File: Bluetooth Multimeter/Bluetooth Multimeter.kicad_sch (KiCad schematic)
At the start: 33 parts, among them J1 V/Ohm, J2 Com, J3 mA, J4 A, J5 Parallel Prot, J6 3.3V, J7 GND, K1 Low Range, K2 Medium Range, K3 High Range, K4 UH Range (Ohm Only), K5 V/Ohm Switch, U1 ItsyBitsy_NRF52840_Big

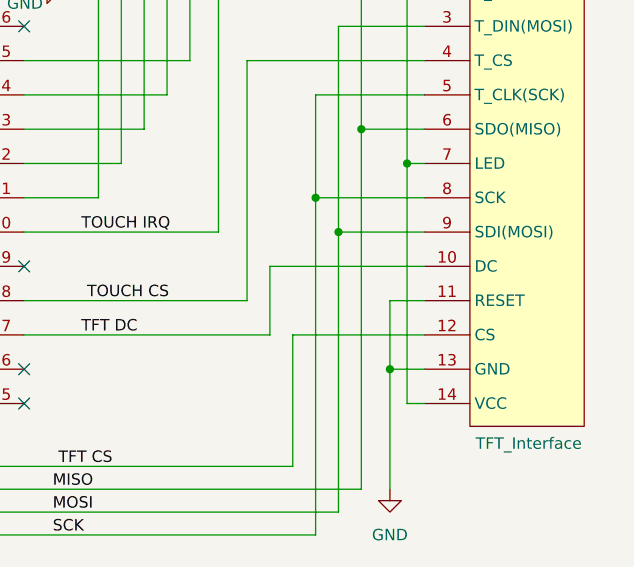
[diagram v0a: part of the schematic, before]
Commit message: fixed itsybitsy footprint and lcd connection
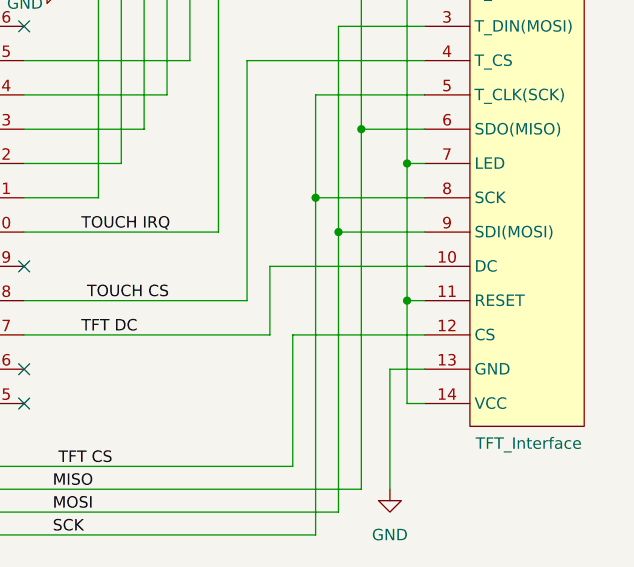
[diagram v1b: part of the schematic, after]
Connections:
- net +3.3V: now also DS1.11 (RESET)
- net GND: no longer DS1.11 (RESET)
- net Speaker Control: no longer U1.
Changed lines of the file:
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@@
   (junction (at 104.775 177.165) (diameter 0) (color 0 0 0 0)
   )
-  (junction (at 231.775 111.76) (diameter 0) (color 0 0 0 0)
-  )
   (junction (at 93.98 28.575) (diameter 0) (color 0 0 0 0)
   )
@@
   )
   (junction (at 107.95 167.005) (diameter 0) (color 0 0 0 0)
+  )
+  (junction (at 233.68 104.14) (diameter 0) (color 0 0 0 0)
   )
   (junction (at 120.65 167.005) (diameter 0) (color 0 0 0 0)
@@
     (stroke (width 0) (type default))
   )
-  (wire (pts (xy 231.775 104.14) (xy 231.775 111.76))
-    (stroke (width 0) (type default))
-  )
   (wire (pts (xy 153.67 100.33) (xy 163.195 100.33))
     (stroke (width 0) (type default))
@@
     (stroke (width 0) (type default))
   )
-  (wire (pts (xy 235.585 104.14) (xy 231.775 104.14))
+  (wire (pts (xy 235.585 104.14) (xy 233.68 104.14))
     (stroke (width 0) (type default))
   )
@@
     (stroke (width 0) (type default))
   )
-  (wire (pts (xy 233.68 88.9) (xy 233.68 115.57))
+  (wire (pts (xy 233.68 88.9) (xy 233.68 104.14))
     (stroke (width 0) (type default))
   )
@@
   )
   (wire (pts (xy 158.115 127.635) (xy 226.06 127.635))
+    (stroke (width 0) (type default))
+  )
+  (wire (pts (xy 233.68 104.14) (xy 233.68 115.57))
     (stroke (width 0) (type default))
   )
@@
       (effects (font (size 1.27 1.27)) hide)
     )
-    (pin "")
     (pin "1")
     (pin "10")

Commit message: pcb modifications based on first shop board
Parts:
- D1, D2, D3, D4: footprint Diode_THT:D_DO-41_SOD81_P10.16mm_Horizontal -> Diode_THT:D_DO-41_SOD81_P7.62mm_Horizontal
- D5, D6, D7, D8, D9: footprint Diode_THT:D_DO-35_SOD27_P7.62mm_Horizontal -> 502ProjectFootprints:D_DO-35_SOD27_P5.08mm_Horizontal
- DS1: footprint 502ProjectFootprints:PinHeader_1x14_P2.54mm_Vertical_H0.9mm -> 502ProjectFootprints:PinHeader_1x14_P2.54mm_Vertical_H1.0
- F2: footprint 502ProjectFootprints:LF124041_4 -> 502ProjectFootprints:LF124041_6
- J1, J2, J3, J4, J6, J7: footprint 502ProjectFootprints:PinHeader_1x01_P2.54mm_Vertical_H0.8mm -> 502ProjectFootprints:PinHeader_1x01_P2.54mm_Vertical_H0.9mm
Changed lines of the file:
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@@
       (effects (font (size 1.27 1.27)) (justify left))
     )
-    (property "Footprint" "Diode_THT:D_DO-35_SOD27_P7.62mm_Horizontal" (at 120.015 127 0)
+    (property "Footprint" "502ProjectFootprints:D_DO-35_SOD27_P5.08mm_Horizontal" (at 120.015 127 0)
       (effects (font (size 1.27 1.27)) hide)
     )
@@
       (effects (font (size 1.27 1.27)) (justify left))
     )
-    (property "Footprint" "Diode_THT:D_DO-35_SOD27_P7.62mm_Horizontal" (at 87.63 143.51 0)
+    (property "Footprint" "502ProjectFootprints:D_DO-35_SOD27_P5.08mm_Horizontal" (at 87.63 143.51 0)
       (effects (font (size 1.27 1.27)) hide)
     )
@@
       (effects (font (size 1.27 1.27)))
     )
-    (property "Footprint" "502ProjectFootprints:PinHeader_1x01_P2.54mm_Vertical_H0.8mm" (at 82.55 153.035 0)
+    (property "Footprint" "502ProjectFootprints:PinHeader_1x01_P2.54mm_Vertical_H0.9mm" (at 82.55 153.035 0)
       (effects (font (size 1.27 1.27)) hide)
     )
@@
       (effects (font (size 1.27 1.27)) (justify left))
     )
-    (property "Footprint" "Diode_THT:D_DO-35_SOD27_P7.62mm_Horizontal" (at 120.015 90.17 0)
+    (property "Footprint" "502ProjectFootprints:D_DO-35_SOD27_P5.08mm_Horizontal" (at 120.015 90.17 0)
       (effects (font (size 1.27 1.27)) hide)
     )
@@
       (effects (font (size 1.27 1.27)) (justify left))
     )
-    (property "Footprint" "502ProjectFootprints:PinHeader_1x14_P2.54mm_Vertical_H0.9mm" (at 239.395 59.69 0)
+    (property "Footprint" "502ProjectFootprints:PinHeader_1x14_P2.54mm_Vertical_H1.0" (at 239.395 59.69 0)
       (effects (font (size 1.27 1.27)) hide)
     )
@@
       (effects (font (size 1.27 1.27)) (justify left))
     )
-    (property "Footprint" "Diode_THT:D_DO-41_SOD81_P10.16mm_Horizontal" (at 114.3 161.29 0)
+    (property "Footprint" "Diode_THT:D_DO-41_SOD81_P7.62mm_Horizontal" (at 114.3 161.29 0)
       (effects (font (size 1.27 1.27)) hide)
     )
@@
       (effects (font (size 1.27 1.27)) (justify left))
     )
-    (property "Footprint" "Diode_THT:D_DO-41_SOD81_P10.16mm_Horizontal" (at 142.875 161.29 0)
+    (property "Footprint" "Diode_THT:D_DO-41_SOD81_P7.62mm_Horizontal" (at 142.875 161.29 0)
       (effects (font (size 1.27 1.27)) hide)
     )
@@
       (effects (font (size 1.27 1.27)) (justify left))
     )
-    (property "Footprint" "Diode_THT:D_DO-41_SOD81_P10.16mm_Horizontal" (at 120.65 161.29 0)
+    (property "Footprint" "Diode_THT:D_DO-41_SOD81_P7.62mm_Horizontal" (at 120.65 161.29 0)
       (effects (font (size 1.27 1.27)) hide)
     )
@@
       (effects (font (size 1.27 1.27)) (justify left))
     )
-    (property "Footprint" "Diode_THT:D_DO-41_SOD81_P10.16mm_Horizontal" (at 136.525 161.29 0)
+    (property "Footprint" "Diode_THT:D_DO-41_SOD81_P7.62mm_Horizontal" (at 136.525 161.29 0)
       (effects (font (size 1.27 1.27)) hide)
     )
@@
       (effects (font (size 1.27 1.27)))
     )
-    (property "Footprint" "502ProjectFootprints:PinHeader_1x01_P2.54mm_Vertical_H0.8mm" (at 82.55 167.005 0)
+    (property "Footprint" "502ProjectFootprints:PinHeader_1x01_P2.54mm_Vertical_H0.9mm" (at 82.55 167.005 0)
       (effects (font (size 1.27 1.27)) hide)
     )
@@
       (effects (font (size 1.27 1.27)))
     )
-    (property "Footprint" "502ProjectFootprints:PinHeader_1x01_P2.54mm_Vertical_H0.8mm" (at 29.21 24.13 0)
+    (property "Footprint" "502ProjectFootprints:PinHeader_1x01_P2.54mm_Vertical_H0.9mm" (at 29.21 24.13 0)
       (effects (font (size 1.27 1.27)) hide)
     )
@@
       (effects (font (size 1.27 1.27)))
     )
-    (property "Footprint" "502ProjectFootprints:PinHeader_1x01_P2.54mm_Vertical_H0.8mm" (at 29.21 30.48 0)
+    (property "Footprint" "502ProjectFootprints:PinHeader_1x01_P2.54mm_Vertical_H0.9mm" (at 29.21 30.48 0)
       (effects (font (size 1.27 1.27)) hide)
     )
@@
       (effects (font (size 1.27 1.27)))
     )
-    (property "Footprint" "502ProjectFootprints:PinHeader_1x01_P2.54mm_Vertical_H0.8mm" (at 82.55 177.165 0)
+    (property "Footprint" "502ProjectFootprints:PinHeader_1x01_P2.54mm_Vertical_H0.9mm" (at 82.55 177.165 0)
       (effects (font (size 1.27 1.27)) hide)
     )
@@
       (effects (font (size 1.27 1.27)) (justify left))
     )
-    (property "Footprint" "Diode_THT:D_DO-35_SOD27_P7.62mm_Horizontal" (at 120.015 54.61 0)
+    (property "Footprint" "502ProjectFootprints:D_DO-35_SOD27_P5.08mm_Horizontal" (at 120.015 54.61 0)
       (effects (font (size 1.27 1.27)) hide)
     )
@@
       (effects (font (size 1.27 1.27)))
     )
-    (property "Footprint" "502ProjectFootprints:LF124041_4" (at 92.075 172.085 0)
+    (property "Footprint" "502ProjectFootprints:LF124041_6" (at 92.075 172.085 0)
       (effects (font (size 1.27 1.27)) hide)
     )
@@
       (effects (font (size 1.27 1.27)) (justify left))
     )
-    (property "Footprint" "Diode_THT:D_DO-35_SOD27_P7.62mm_Horizontal" (at 120.015 22.86 0)
+    (property "Footprint" "502ProjectFootprints:D_DO-35_SOD27_P5.08mm_Horizontal" (at 120.015 22.86 0)
       (effects (font (size 1.27 1.27)) hide)
     )
@@
       (effects (font (size 1.27 1.27)))
     )
-    (property "Footprint" "502ProjectFootprints:PinHeader_1x01_P2.54mm_Vertical_H0.8mm" (at 83.185 28.575 0)
-      (effects (font (size 1.27 1.27)) hide)
-    )
+    (property "Footprint" "502ProjectFootprints:PinHeader_1x01_P2.54mm_Vertical_H0.9mm" (at 83.185 28.575 0)
+      (effects (font (size 1.27 1.27)) hide)
+    )

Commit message: finalized rev 2 board to be milled
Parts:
- F1: footprint 502ProjectFootprints:LF124061_1 -> 502ProjectFootprints:LF124061_3
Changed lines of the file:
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@@
       (effects (font (size 1.27 1.27)))
     )
-    (property "Footprint" "502ProjectFootprints:LF124061_1" (at 92.075 161.925 0)
+    (property "Footprint" "502ProjectFootprints:LF124061_3" (at 92.075 161.925 0)
       (effects (font (size 1.27 1.27)) hide)
     )

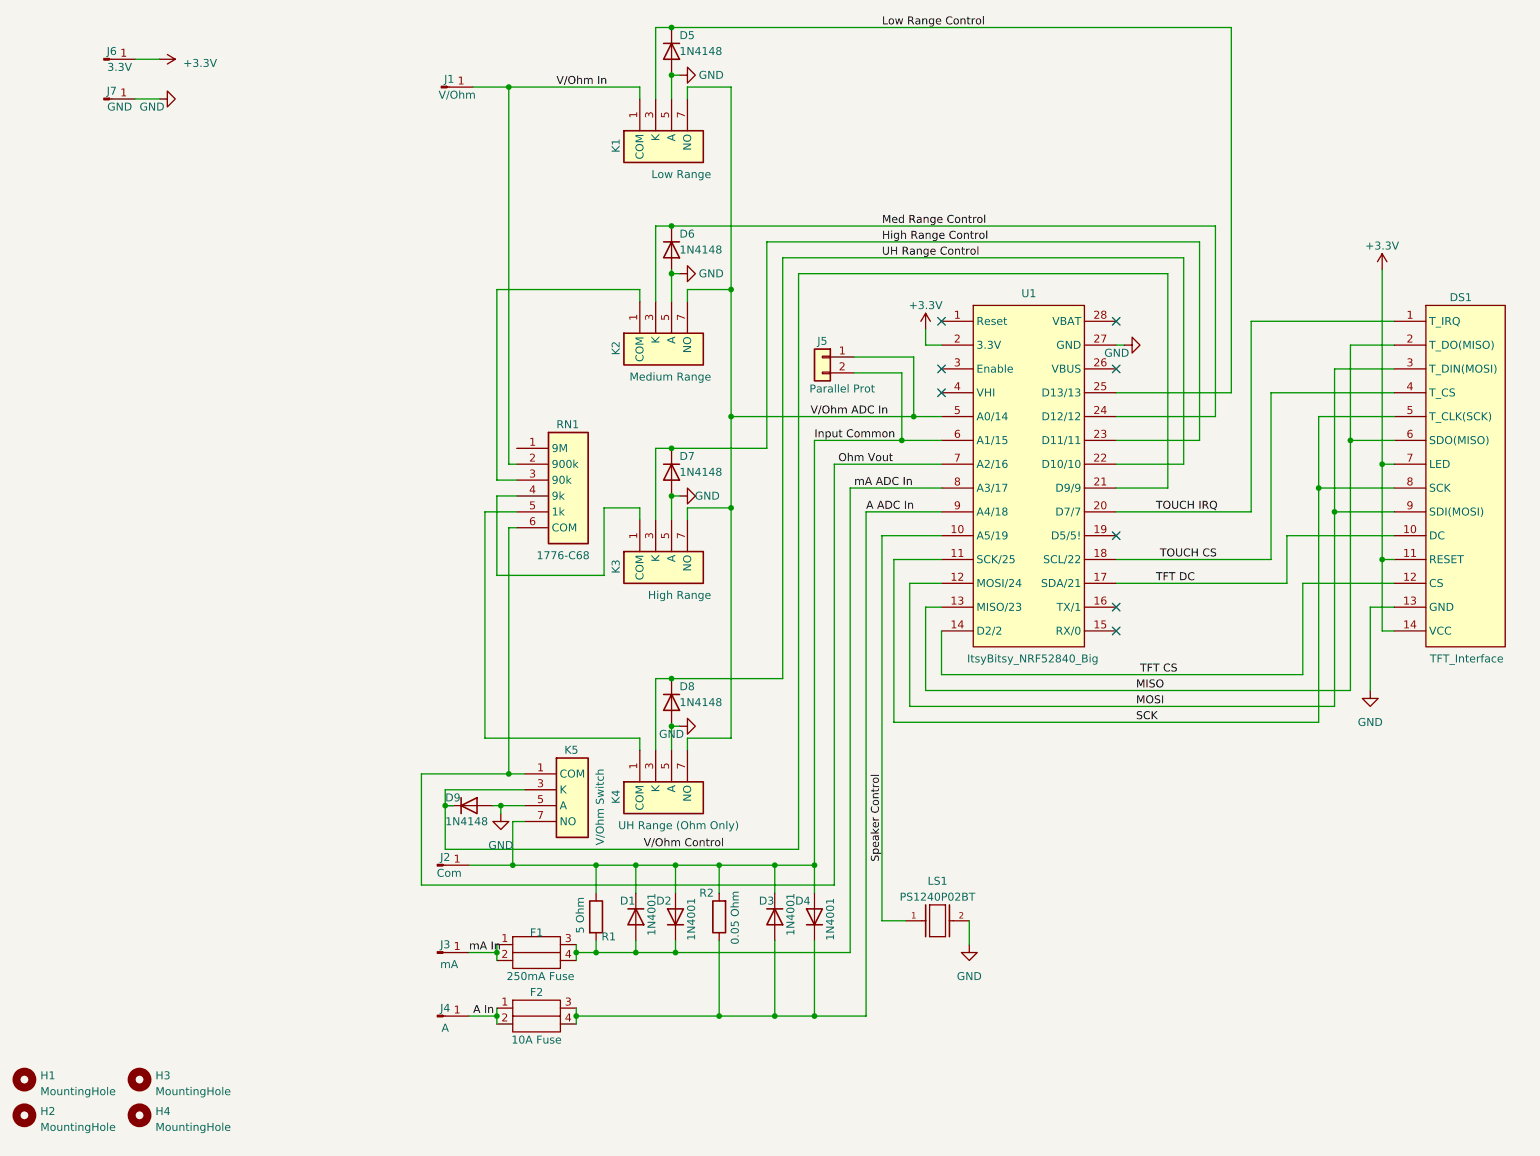
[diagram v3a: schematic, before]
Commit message: made inverted connector PCB main project, fixed ohmeter
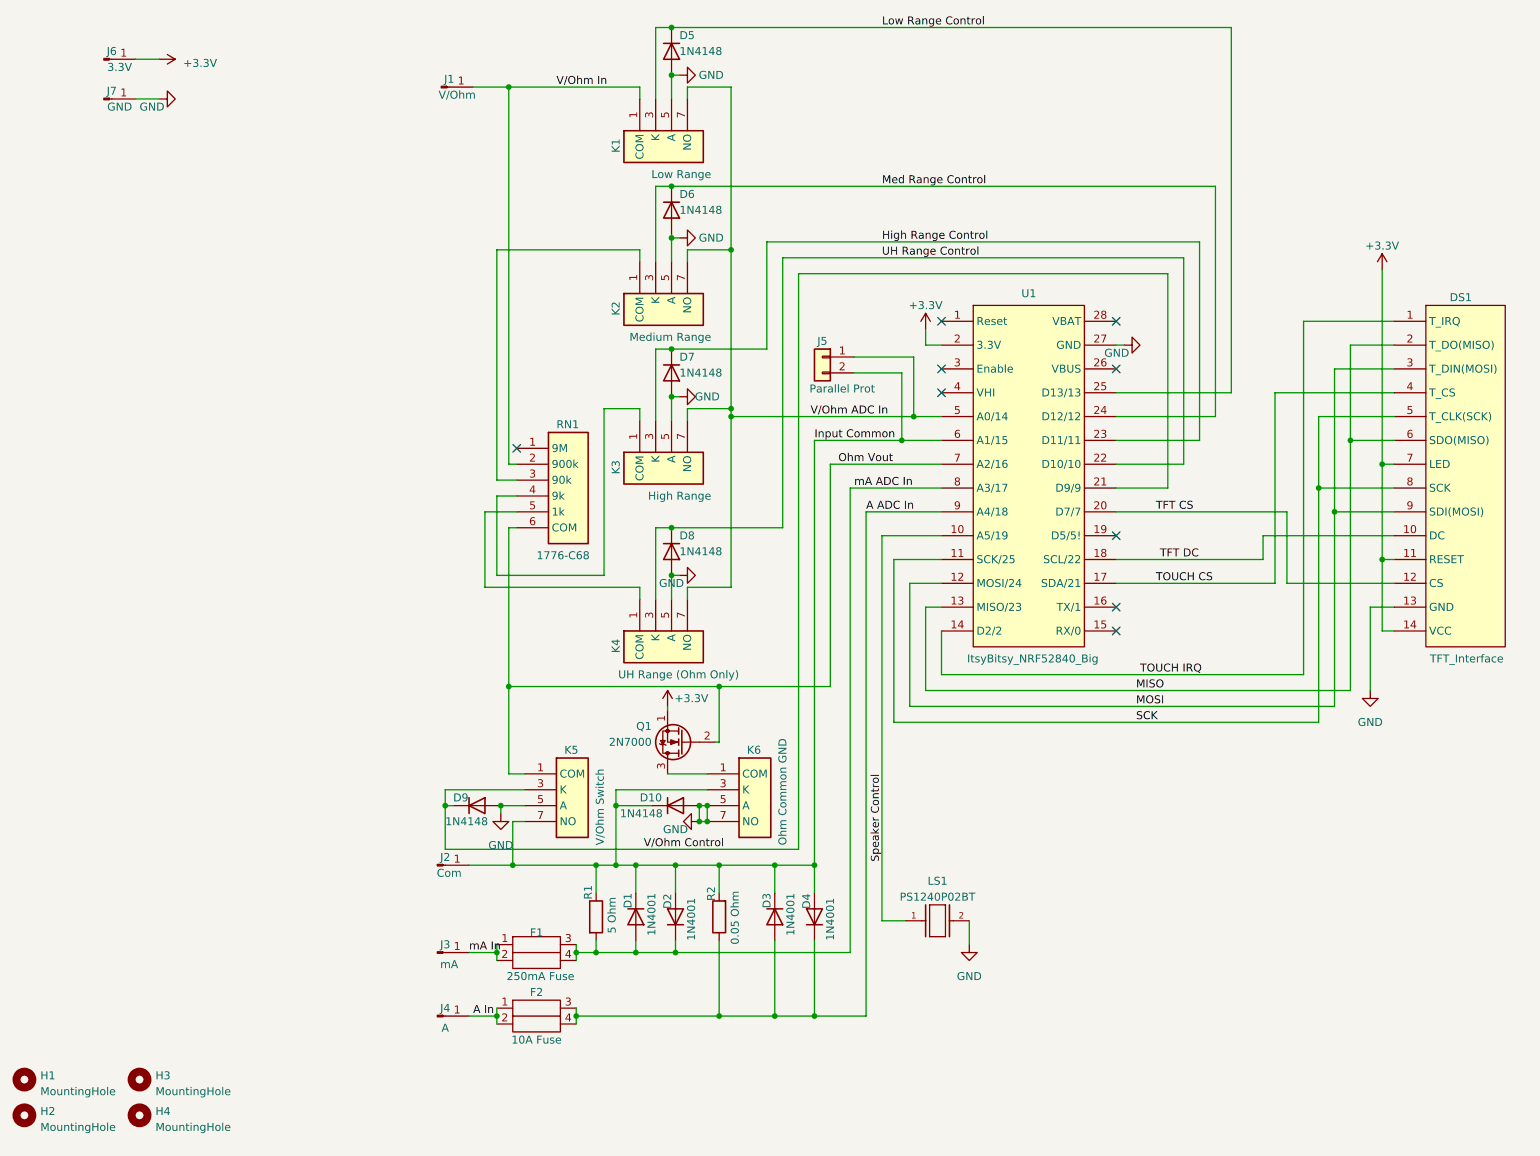
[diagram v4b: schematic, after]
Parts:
- added D10: 1N4148, 502ProjectFootprints:D_DO-35_SOD27_P5.08mm_Horizontal, symbol Diode:1N4148
- added K6: Ohm Common GND, 502ProjectFootprints:SIL03-1A72-71_4, symbol 502ProjectSymbols:SIL03-1A72-71D
- added Q1: 2N7000, Package_TO_SOT_THT:TO-92_Inline, symbol Transistor_FET:2N7000
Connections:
- net +3.3V: now also Q1.1 (S)
- net GND: now also D10.2 (A), K6.5 (A), K6.7 (NO)
- net Input Common: now also D10.1 (K), K6.3 (K)
- net Ohm Vout: now also Q1.2 (G)
- net TFT CS: now also U1.20 (D7/7); no longer U1.14 (D2/2)
- net TFT DC: now also U1.18 (SCL/22); no longer U1.17 (SDA/21)
- net TOUCH CS: now also U1.17 (SDA/21); no longer U1.18 (SCL/22)
- net TOUCH IRQ: now also U1.14 (D2/2); no longer U1.20 (D7/7)
- new net: K6.1 (COM), Q1.3 (D)
- no-connect marks 8 -> 9
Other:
- moved on the sheet: D6, D7, D8, D9, K2, K3, K4

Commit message: rerouted board for external fab
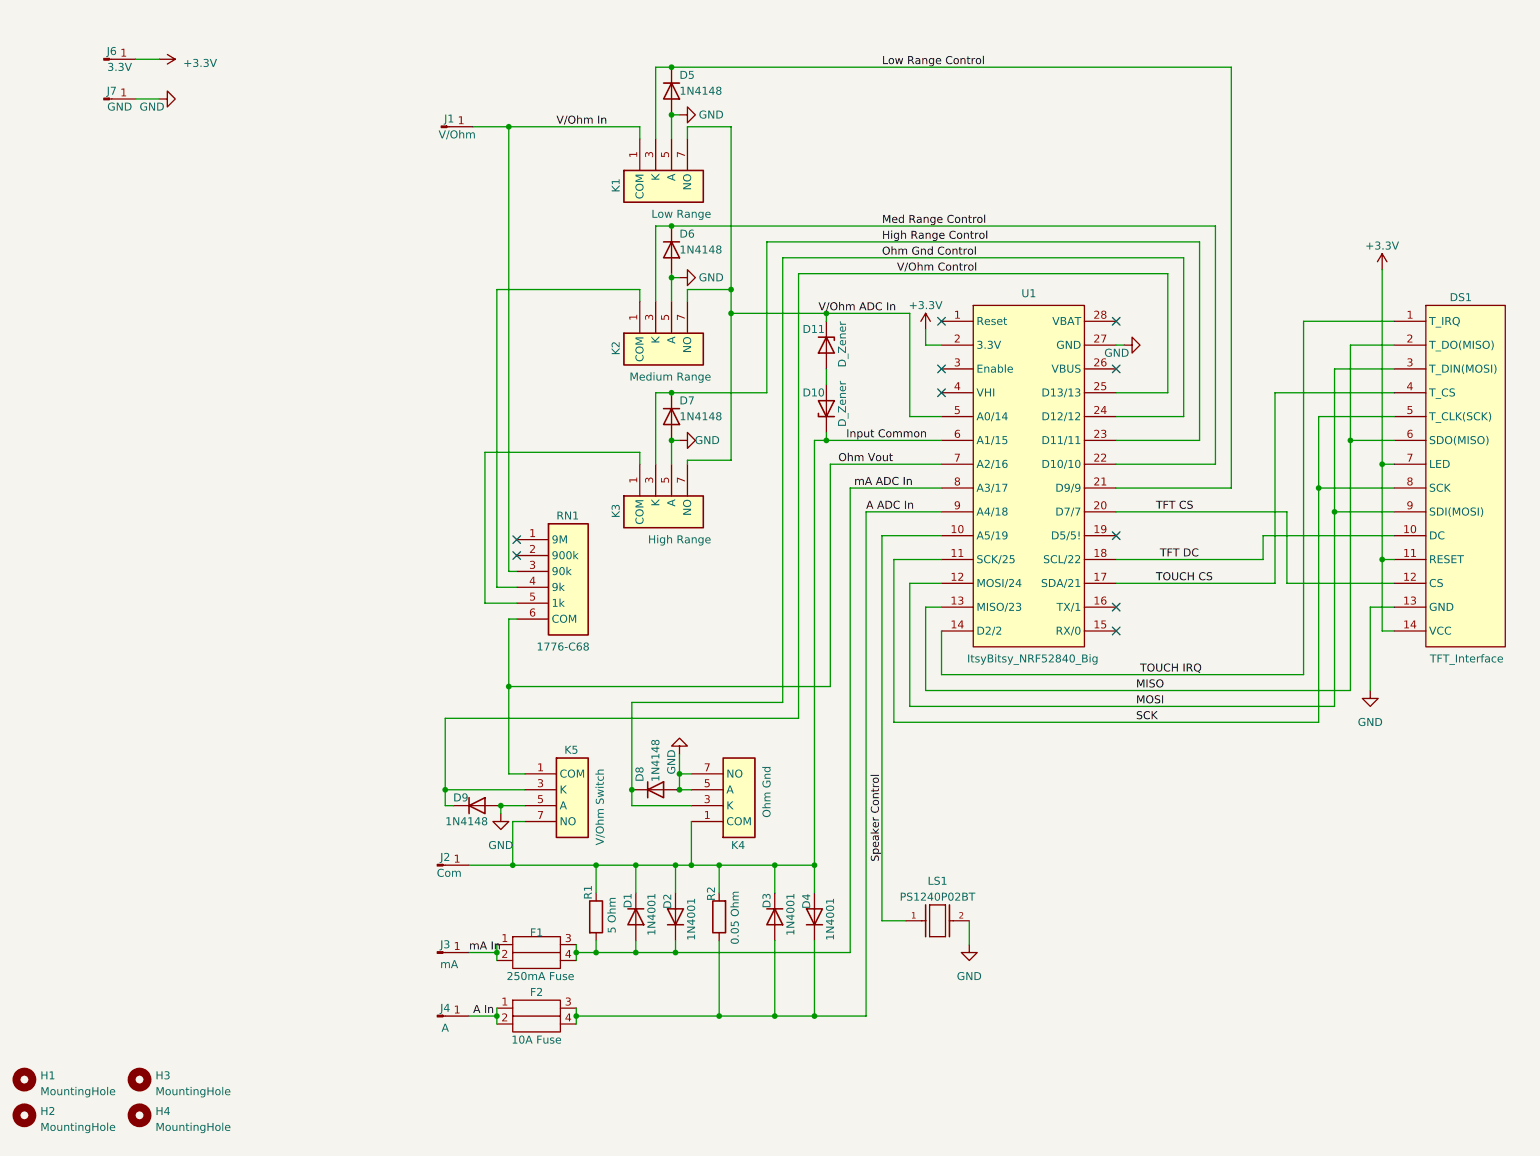
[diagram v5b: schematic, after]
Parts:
- removed D10: 1N4148, 502ProjectFootprints:D_DO-35_SOD27_P5.08mm_Horizontal, symbol Diode:1N4148
- removed J5: Parallel Prot, 502ProjectFootprints:PinHeader_1x02_P2.54mm_Vertical_H0.9mm, symbol Connector_Generic:Conn_01x02
- removed K6: Ohm Common GND, 502ProjectFootprints:SIL03-1A72-71_4, symbol 502ProjectSymbols:SIL03-1A72-71D
- removed Q1: 2N7000, Package_TO_SOT_THT:TO-92_Inline, symbol Transistor_FET:2N7000
- added D10, D11: D_Zener, Diode_THT:D_DO-35_SOD27_P7.62mm_Horizontal, symbol Device:D_Zener
- K4: value UH Range (Ohm Only) -> Ohm Gnd
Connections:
- net GND: now also K4.7 (NO)
- net Input Common: now also K4.1 (COM), D10.1 (K)
- net Low Range Control: now also U1.21 (D9/9); no longer U1.25 (D13/13)
- net Med Range Control: now also U1.22 (D10/10); no longer U1.24 (D12/12)
- net V/Ohm ADC In: now also D11.1 (K); no longer K4.7 (NO)
- net V/Ohm Control: now also U1.25 (D13/13); no longer U1.21 (D9/9)
- net V/Ohm In: now also RN1.3 (90k); no longer RN1.2 (900k)
- net at K2.1 (COM): now also RN1.4 (9k); no longer RN1.3 (90k)
- net at K3.1 (COM): now also RN1.5 (1k); no longer RN1.4 (9k)
- net UH Range Control renamed Ohm Gnd Control
- net Ohm Gnd Control: now also U1.24 (D12/12); no longer U1.22 (D10/10)
- new net: D10.2 (A), D11.2 (A)
- no-connect marks 9 -> 10
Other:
- moved on the sheet: D5, D6, D7, D8, J1, K1, K2, K3, K4, RN1
